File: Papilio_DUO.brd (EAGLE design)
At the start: 100 x 56 mm, 125 parts, among them IC1 FT2232H, SW1 SWITCH-2CH-6P-3010010P1, SW2 EVQQ2, T100 MOSFET-NCHANNELSMD, U1 ARDUINO_MEGA_SHIELD, U100 PCA9306, U101 ATMEGA32U4-XUMU, U2 LTC3419EMS, U3 93C46B, X1 12MHz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

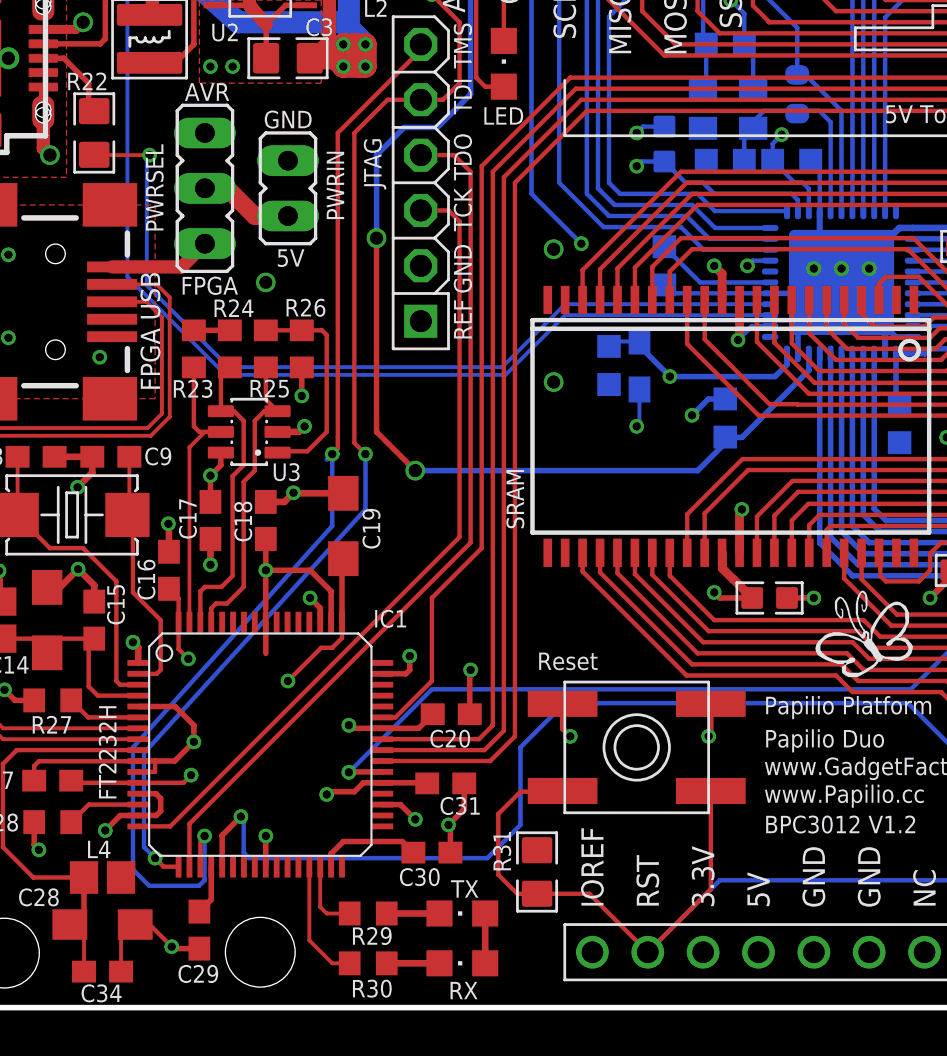
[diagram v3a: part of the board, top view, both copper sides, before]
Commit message: Routing changes: VBUS connected, RX/TX LED's connected to port B instead of A.
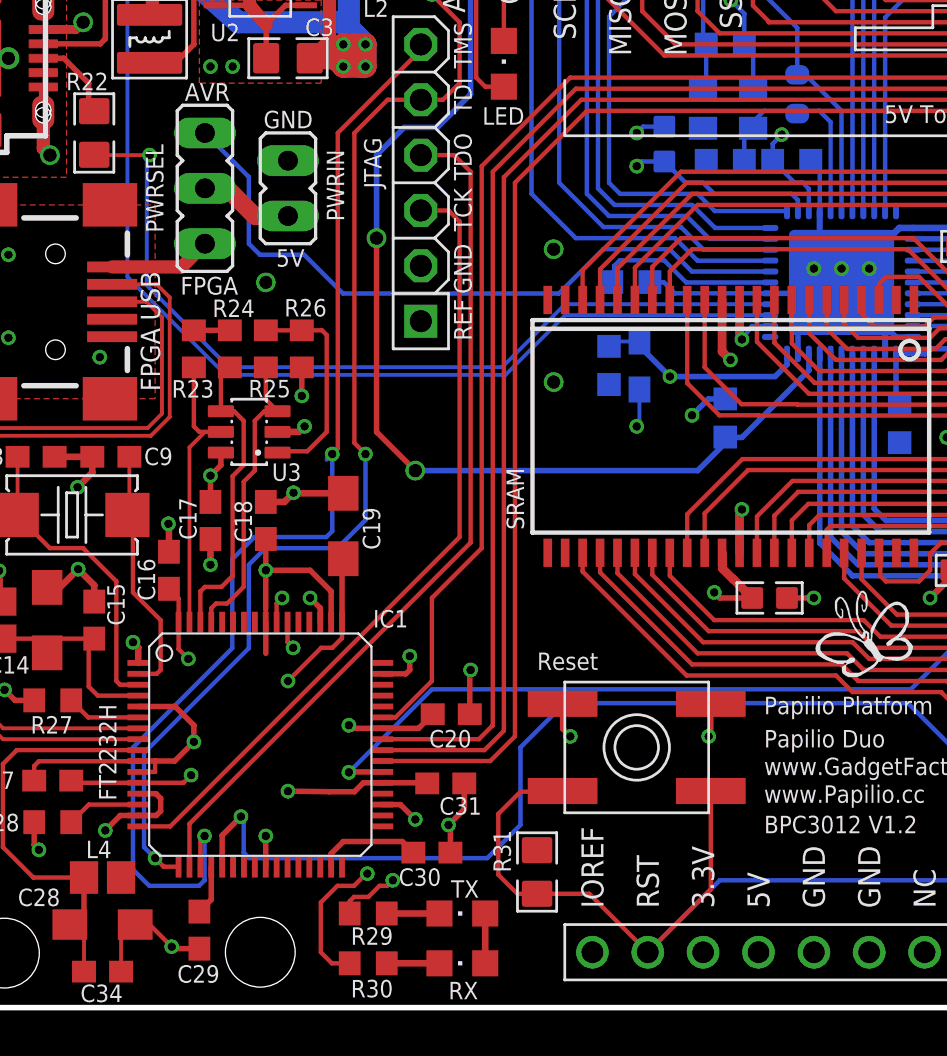
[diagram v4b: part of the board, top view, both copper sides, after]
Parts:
- moved C103 1.71 mm to (31.2, 33.3), turned to 180 degrees
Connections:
- net 5V_ARDUINO: now also U101.7
- net AC3: no longer R30.1
- net AC4: no longer R29.1
- net BC3: now also R30.1
- net BC4: now also R29.1
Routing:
- net 5V_ARDUINO: track 9.91 -> 42.0 mm
- net BC3: track 0.00 -> 19.5 mm, vias 0 -> 2
- net BC4: track 0.00 -> 19.2 mm, vias 0 -> 2
- net AC3: track 5.67 -> 0.00 mm
- net AC4: track 3.33 -> 0.00 mm
- net GND: track 238.2 -> 241.4 mm
- net UCAP: track 5.53 -> 8.47 mm
- net AD1-JTAG_TDI: track 102.2 -> 104.5 mm
- net AD3-JTAG_TMS: track 106.5 -> 108.7 mm
- net D3: track 20.2 -> 21.2 mm
- net 1.8V: track 38.6 -> 39.4 mm
- net D2: track 19.1 -> 19.8 mm
- net ATMEGA_IO10*: track 39.7 -> 39.2 mm, vias 2 -> 0

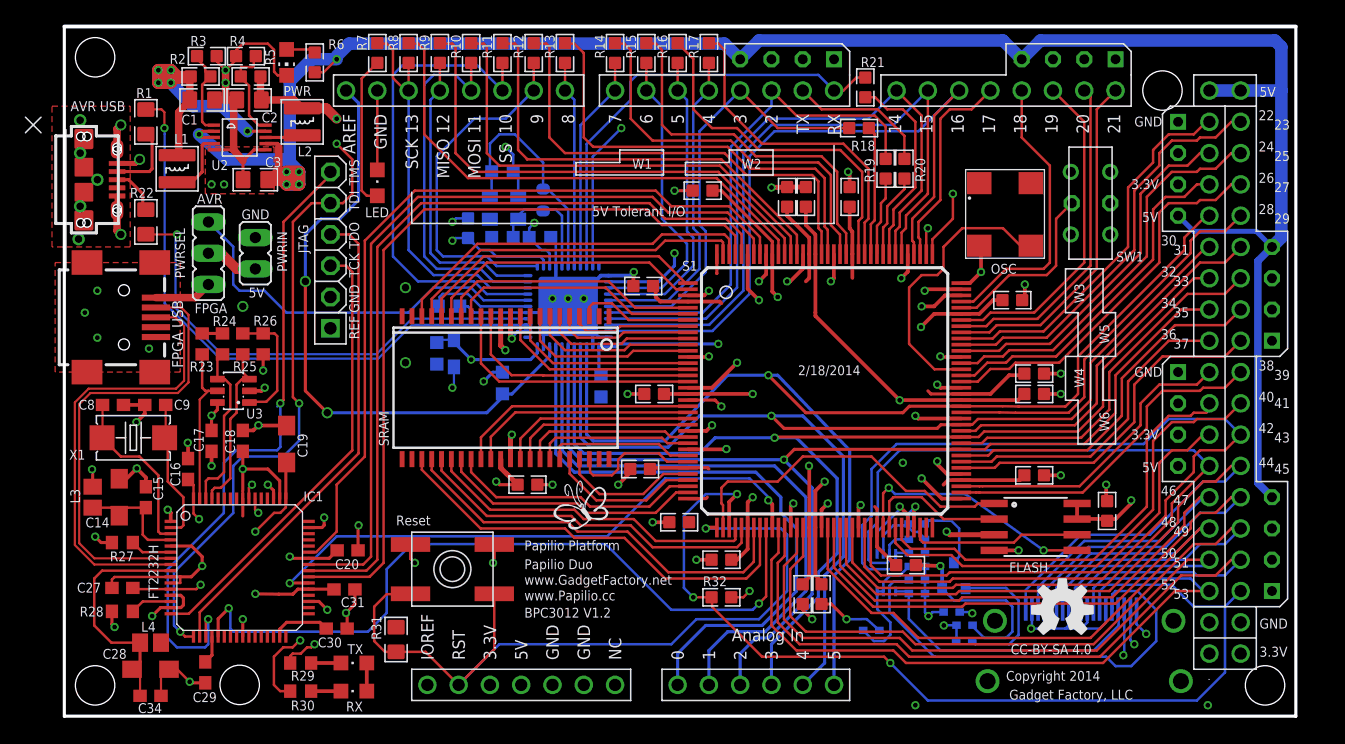
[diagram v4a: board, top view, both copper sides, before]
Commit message: Silkscreen fixes, Reset re-worked so RST pin resets atmega32u4 instead of FPGA.
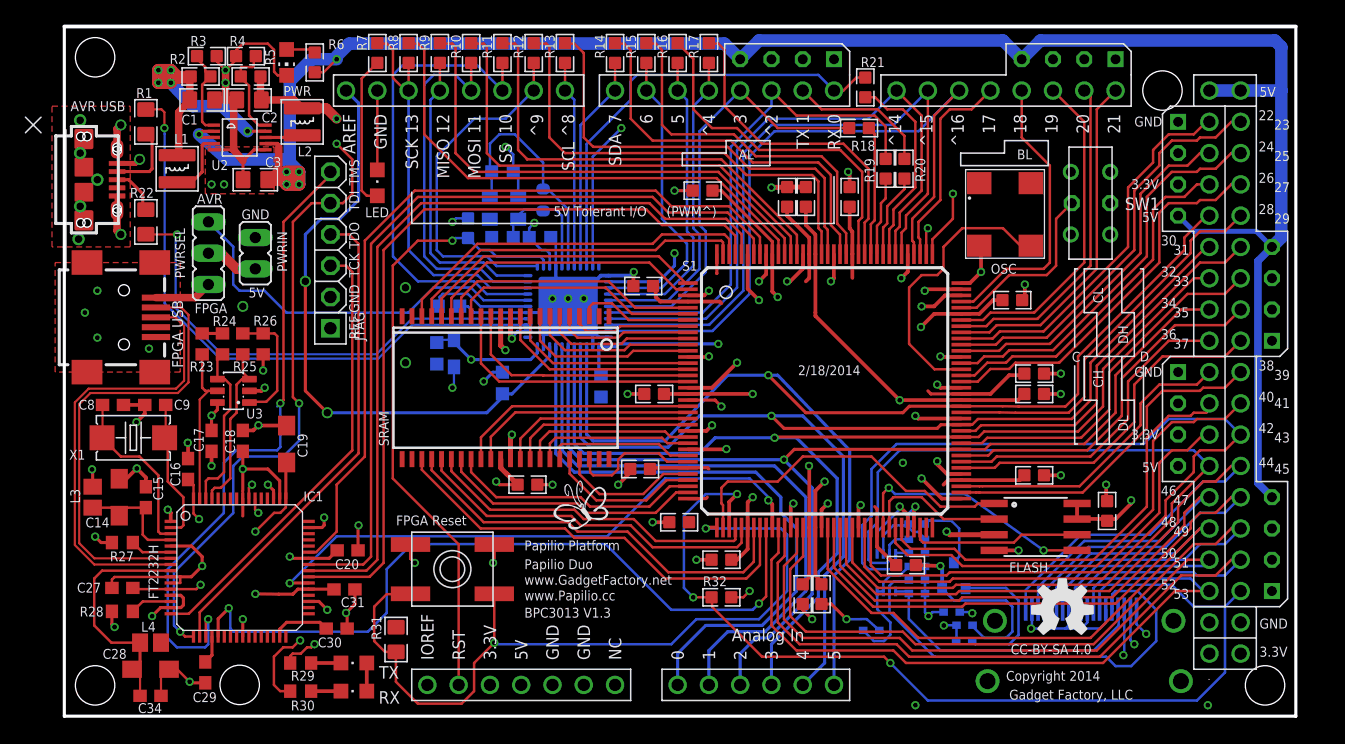
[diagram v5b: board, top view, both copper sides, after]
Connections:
- net ARD_RESET: now also U1.RES
- net RESET: no longer U1.RES
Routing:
- net ARD_RESET: track 41.0 -> 82.9 mm
- net RESET: track 65.3 -> 64.8 mm, vias 1 -> 2
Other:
- board text added: "AL"
- board text added: "BL"
- board text added: "BPC3013 V1.3"
- board text added: "C"
- board text added: "CH"
- board text added: "CL"
- board text added: "D"
- board text added: "DH"
- board text added: "DL"
- board text added: "FPGA Reset"
- board text removed: "BPC3012 V1.2"
- board text removed: "Reset"
- board text removed: "W1"
- board text removed: "W2"
- board text removed: "W3"
- board text removed: "W4"
- board text removed: "W5"
- board text removed: "W6"

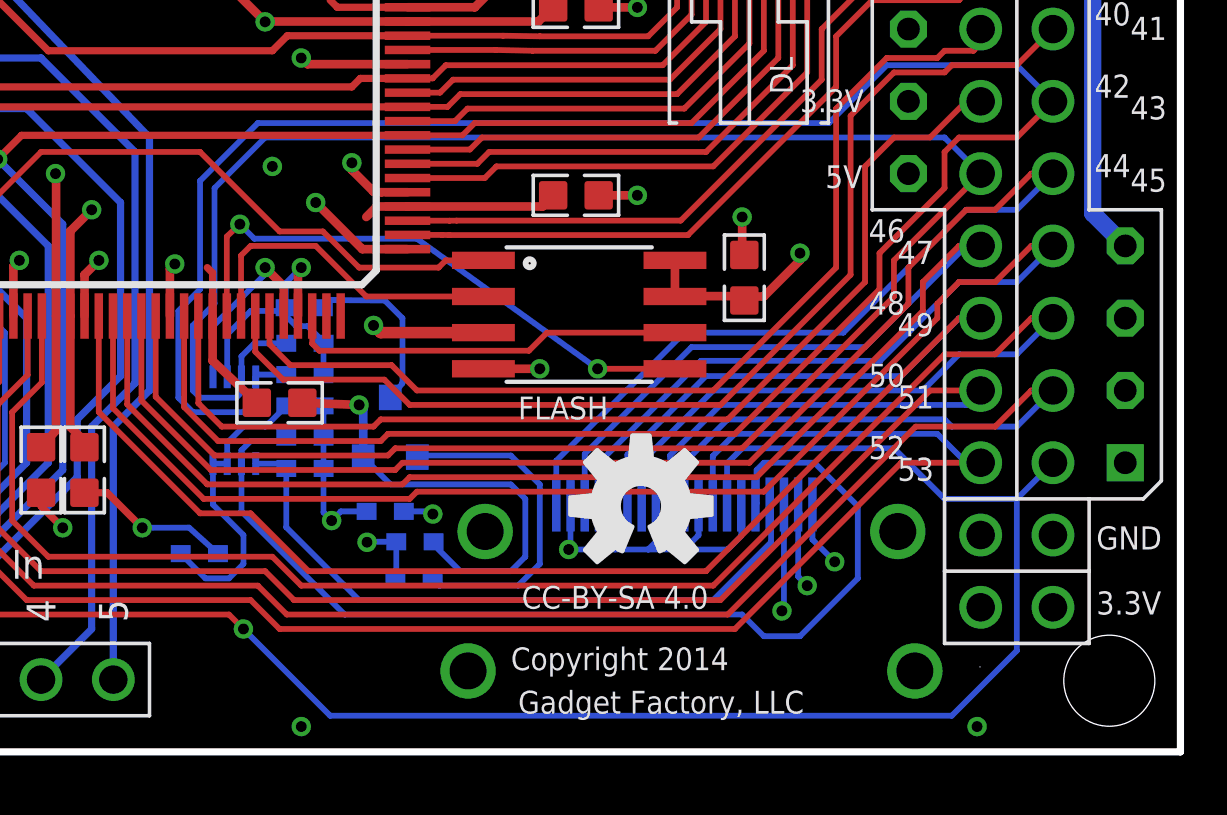
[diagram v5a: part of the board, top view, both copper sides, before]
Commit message: Remove HDMI
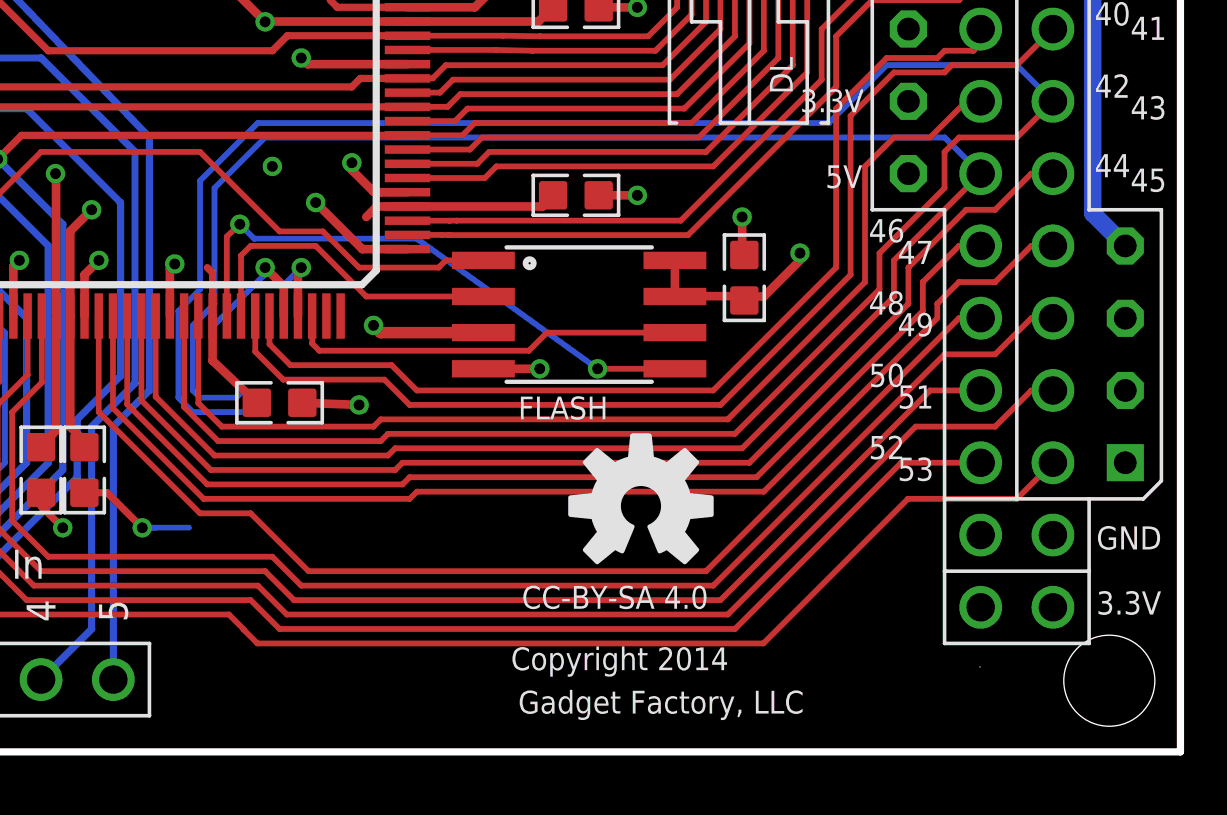
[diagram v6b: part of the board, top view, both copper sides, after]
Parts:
- removed C100: 1uF, saanlima:0402
- removed HDMI: HDMI-TYPE-A-RECEPTICALFCI10029449, saanlima:FCI-HDMI-TYPE-A-RECEPT
- removed R100, R101: 10K, saanlima:0402
- removed R102: 0, saanlima:0402
- removed R103, R104, R106, R107: 1K, saanlima:0402
- removed R105: 100K, saanlima:0402
- removed R108: 2.2K, saanlima:0402
- removed T100: MOSFET-NCHANNELSMD, saanlima:SOT23-3
- removed U100: PCA9306, saanlima:PSOP-8
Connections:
- removed net DDC_SCL: HDMI.15, R104.2, U100.6
- removed net DDC_SDA: HDMI.16, R103.2, U100.5
- removed net DETECT: HDMI.19, R100.2, R101.1
- removed net HDMI_DET#: R108.2, T100.3
- removed net N$17: R101.2, T100.1
- removed net N$6: C100.1, R105.1, U100.7, U100.8
- removed net TX_HDMI_5V: HDMI.18, R102.1, R103.1, R104.1, R105.2
- net 3V3: no longer R106.1, R107.1, R108.1, U100.2
- net 5V0: no longer R102.2
- net GND: no longer C100.2, HDMI.11, HDMI.14, HDMI.17, HDMI.2, HDMI.5, HDMI.8, R100.1, T100.2, U100.1
- net MEGA_D43: no longer R106.2, U100.4
- net MEGA_D44: no longer R107.2, U100.3
- net MEGA_D45: no longer HDMI.1
- net MEGA_D46: no longer HDMI.3
- net MEGA_D47: no longer HDMI.4
- net MEGA_D48: no longer HDMI.6
- net MEGA_D49: no longer HDMI.7
- net MEGA_D50: no longer HDMI.9
- net MEGA_D51: no longer HDMI.10
- net MEGA_D52: no longer HDMI.12
- net MEGA_D53: no longer HDMI.13
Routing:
- net DDC_SCL: track 36.3 -> 0.00 mm
- net GND: track 241.4 -> 205.5 mm, vias 76 -> 74
- net TX_HDMI_5V: track 27.4 -> 0.00 mm, vias 2 -> 0
- net DDC_SDA: track 23.5 -> 0.00 mm
- net MEGA_D45: track 64.2 -> 41.1 mm
- net DETECT: track 22.0 -> 0.00 mm, vias 2 -> 0
- net MEGA_D47: track 62.1 -> 41.6 mm
- net MEGA_D46: track 57.0 -> 38.3 mm
- net MEGA_D49: track 67.1 -> 49.0 mm
- net MEGA_D53: track 82.7 -> 64.9 mm, vias 3 -> 2
- net MEGA_D48: track 56.5 -> 40.4 mm
- net MEGA_D51: track 65.6 -> 49.9 mm
- net MEGA_D50: track 60.1 -> 46.5 mm
- net MEGA_D52: track 59.3 -> 47.4 mm
- net N$17: track 11.7 -> 0.00 mm
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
